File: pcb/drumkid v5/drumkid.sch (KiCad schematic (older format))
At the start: 51 parts, among them J5 Conn_01x05_Female, J6 Conn_01x04_Female, J7 Conn_01x06_Female, J8 Conn_01x05_Female, J9 AudioJack3_Ground_Switch, SW1 SW_SPDT, SW2 SW_Push, SW3 SW_Push, SW4 SW_Push, SW5 SW_Push, SW6 SW_Push, SW7 SW_Push, U2 ATmega328P-PU, U3 LM386, Y1 Crystal

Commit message: tidying up repo
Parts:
- C1, C2, C3, C7: renamed from C?; footprint (none) -> Capacitor_THT:C_Disc_D3.4mm_W2.1mm_P2.50mm
- J1: renamed from J?; footprint (none) -> Connector_PinHeader_2.54mm:PinHeader_1x02_P2.54mm_Vertical
- R1, R12, R13, R8: renamed from R?; footprint (none) -> Resistor_THT:R_Axial_DIN0207_L6.3mm_D2.5mm_P10.16mm_Horizontal
- RV1, RV2, RV3, RV4, RV5: footprint Potentiometer_THT:Potentiometer_Alps_RK09K_Single_Vertical -> drumkidcustom:Potentiometer_Alps_RK09K_Single_Vertical
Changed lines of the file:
@@
 F 0 "RV2" H 10230 3004 50  0000 R CNN
 F 1 "R_POT" H 10230 3095 50  0000 R CNN
-F 2 "Potentiometer_THT:Potentiometer_Alps_RK09K_Single_Vertical" H 10300 3050 50  0001 C CNN
+F 2 "drumkidcustom:Potentiometer_Alps_RK09K_Single_Vertical" H 10300 3050 50  0001 C CNN
 F 3 "~" H 10300 3050 50  0001 C CNN
 	1    10300 3050
@@
 F 0 "RV3" H 10230 3504 50  0000 R CNN
 F 1 "R_POT" H 10230 3595 50  0000 R CNN
-F 2 "Potentiometer_THT:Potentiometer_Alps_RK09K_Single_Vertical" H 10300 3550 50  0001 C CNN
+F 2 "drumkidcustom:Potentiometer_Alps_RK09K_Single_Vertical" H 10300 3550 50  0001 C CNN
 F 3 "~" H 10300 3550 50  0001 C CNN
 	1    10300 3550
@@
 F 0 "RV4" H 10230 4004 50  0000 R CNN
 F 1 "R_POT" H 10230 4095 50  0000 R CNN
-F 2 "Potentiometer_THT:Potentiometer_Alps_RK09K_Single_Vertical" H 10300 4050 50  0001 C CNN
+F 2 "drumkidcustom:Potentiometer_Alps_RK09K_Single_Vertical" H 10300 4050 50  0001 C CNN
 F 3 "~" H 10300 4050 50  0001 C CNN
 	1    10300 4050
@@
 F 0 "RV1" V 6243 850 50  0000 C CNN
 F 1 "10k" V 6334 850 50  0000 C CNN
-F 2 "Potentiometer_THT:Potentiometer_Alps_RK09K_Single_Vertical" H 6450 850 50  0001 C CNN
+F 2 "drumkidcustom:Potentiometer_Alps_RK09K_Single_Vertical" H 6450 850 50  0001 C CNN
 F 3 "~" H 6450 850 50  0001 C CNN
 	1    6450 850
@@
 F 0 "RV5" H 10230 4504 50  0000 R CNN
 F 1 "R_POT" H 10230 4595 50  0000 R CNN
-F 2 "Potentiometer_THT:Potentiometer_Alps_RK09K_Single_Vertical" H 10300 4550 50  0001 C CNN
+F 2 "drumkidcustom:Potentiometer_Alps_RK09K_Single_Vertical" H 10300 4550 50  0001 C CNN
 F 3 "~" H 10300 4550 50  0001 C CNN
 	1    10300 4550
@@
 	6950 1900 7150 1900
 $Comp
-L Connector:Conn_01x02_Female J?
+L Connector:Conn_01x02_Female J1
 U 1 1 5D8A22D2
 P 3500 5400
-F 0 "J?" H 3527 5376 50  0000 L CNN
+F 0 "J1" H 3527 5376 50  0000 L CNN
 F 1 "Conn_01x02_Female" H 3527 5285 50  0000 L CNN
-F 2 "" H 3500 5400 50  0001 C CNN
+F 2 "Connector_PinHeader_2.54mm:PinHeader_1x02_P2.54mm_Vertical" H 3500 5400 50  0001 C CNN
 F 3 "~" H 3500 5400 50  0001 C CNN
 	1    3500 5400
@@
 	3100 5500 3100 5700
 $Comp
-L Device:R R?
+L Device:R R1
 U 1 1 5D8A7D99
 P 4650 850
-F 0 "R?" V 4443 850 50  0000 C CNN
+F 0 "R1" V 4443 850 50  0000 C CNN
 F 1 "220" V 4534 850 50  0000 C CNN
-F 2 "" V 4580 850 50  0001 C CNN
+F 2 "Resistor_THT:R_Axial_DIN0207_L6.3mm_D2.5mm_P10.16mm_Horizontal" V 4580 850 50  0001 C CNN
 F 3 "~" H 4650 850 50  0001 C CNN
 	1    4650 850
@@
 $EndComp
 $Comp
-L Device:R R?
+L Device:R R8
 U 1 1 5D8A7E6C
 P 5450 850
-F 0 "R?" V 5243 850 50  0000 C CNN
+F 0 "R8" V 5243 850 50  0000 C CNN
 F 1 "680" V 5334 850 50  0000 C CNN
-F 2 "" V 5380 850 50  0001 C CNN
+F 2 "Resistor_THT:R_Axial_DIN0207_L6.3mm_D2.5mm_P10.16mm_Horizontal" V 5380 850 50  0001 C CNN
 F 3 "~" H 5450 850 50  0001 C CNN
 	1    5450 850
@@
 $EndComp
 $Comp
-L Device:R R?
+L Device:R R12
 U 1 1 5D8A7F2E
 P 5850 850
-F 0 "R?" V 5643 850 50  0000 C CNN
+F 0 "R12" V 5643 850 50  0000 C CNN
 F 1 "680" V 5734 850 50  0000 C CNN
-F 2 "" V 5780 850 50  0001 C CNN
+F 2 "Resistor_THT:R_Axial_DIN0207_L6.3mm_D2.5mm_P10.16mm_Horizontal" V 5780 850 50  0001 C CNN
 F 3 "~" H 5850 850 50  0001 C CNN
 	1    5850 850
@@
 $EndComp
 $Comp
-L Device:C C?
+L Device:C C1
 U 1 1 5D8A800B
 P 4850 1150
-F 0 "C?" H 4965 1196 50  0000 L CNN
+F 0 "C1" H 4965 1196 50  0000 L CNN
 F 1 "220nF" H 4965 1105 50  0000 L CNN
-F 2 "" H 4888 1000 50  0001 C CNN
+F 2 "Capacitor_THT:C_Disc_D3.4mm_W2.1mm_P2.50mm" H 4888 1000 50  0001 C CNN
 F 3 "~" H 4850 1150 50  0001 C CNN
 	1    4850 1150
@@
 $EndComp
 $Comp
-L Device:C C?
+L Device:C C3
 U 1 1 5D8BB366
 P 5650 1150
-F 0 "C?" H 5765 1196 50  0000 L CNN
+F 0 "C3" H 5765 1196 50  0000 L CNN
 F 1 "1nF" H 5765 1105 50  0000 L CNN
-F 2 "" H 5688 1000 50  0001 C CNN
+F 2 "Capacitor_THT:C_Disc_D3.4mm_W2.1mm_P2.50mm" H 5688 1000 50  0001 C CNN
 F 3 "~" H 5650 1150 50  0001 C CNN
 	1    5650 1150
@@
 	6000 850  6050 850
 $Comp
-L Device:C C?
+L Device:C C7
 U 1 1 5D8C53A5
 P 6050 1150
-F 0 "C?" H 6165 1196 50  0000 L CNN
+F 0 "C7" H 6165 1196 50  0000 L CNN
 F 1 "220nF" H 6165 1105 50  0000 L CNN
-F 2 "" H 6088 1000 50  0001 C CNN
+F 2 "Capacitor_THT:C_Disc_D3.4mm_W2.1mm_P2.50mm" H 6088 1000 50  0001 C CNN
 F 3 "~" H 6050 1150 50  0001 C CNN
 	1    6050 1150
@@
 $EndComp
 $Comp
-L Device:C C?
+L Device:C C2
 U 1 1 5D8C5552
 P 5250 1150
-F 0 "C?" H 5365 1196 50  0000 L CNN
+F 0 "C2" H 5365 1196 50  0000 L CNN
 F 1 "220nF" H 5365 1105 50  0000 L CNN
-F 2 "" H 5288 1000 50  0001 C CNN
+F 2 "Capacitor_THT:C_Disc_D3.4mm_W2.1mm_P2.50mm" H 5288 1000 50  0001 C CNN
 F 3 "~" H 5250 1150 50  0001 C CNN
 	1    5250 1150
@@
 	6050 1450 6050 1300
 $Comp
-L Device:R R?
+L Device:R R13
 U 1 1 5D8CABE9
 P 6050 1650
-F 0 "R?" H 6120 1696 50  0000 L CNN
+F 0 "R13" H 6120 1696 50  0000 L CNN
 F 1 "330" H 6120 1605 50  0000 L CNN
-F 2 "" V 5980 1650 50  0001 C CNN
+F 2 "Resistor_THT:R_Axial_DIN0207_L6.3mm_D2.5mm_P10.16mm_Horizontal" V 5980 1650 50  0001 C CNN
 F 3 "~" H 6050 1650 50  0001 C CNN
 	1    6050 1650
@@
 	4850 1300 4850 1900
 Wire Wire Line
-	4850 1900 5650 1900
+	4850 1900 5300 1900
 Connection ~ 4850 1900
 Wire Wire Line
@@
 Wire Wire Line
 	6050 850  6300 850
+$Comp
+L power:PWR_FLAG #FLG0101
+U 1 1 5D8894D3
+P 5300 1900
+F 0 "#FLG0101" H 5300 1975 50  0001 C CNN
+F 1 "PWR_FLAG" H 5300 2074 50  0000 C CNN
+F 2 "" H 5300 1900 50  0001 C CNN
+F 3 "~" H 5300 1900 50  0001 C CNN
+	1    5300 1900
+	1    0    0    -1
+$EndComp
+Connection ~ 5300 1900
+Wire Wire Line
+	5300 1900 5650 1900
 $EndSCHEMATC

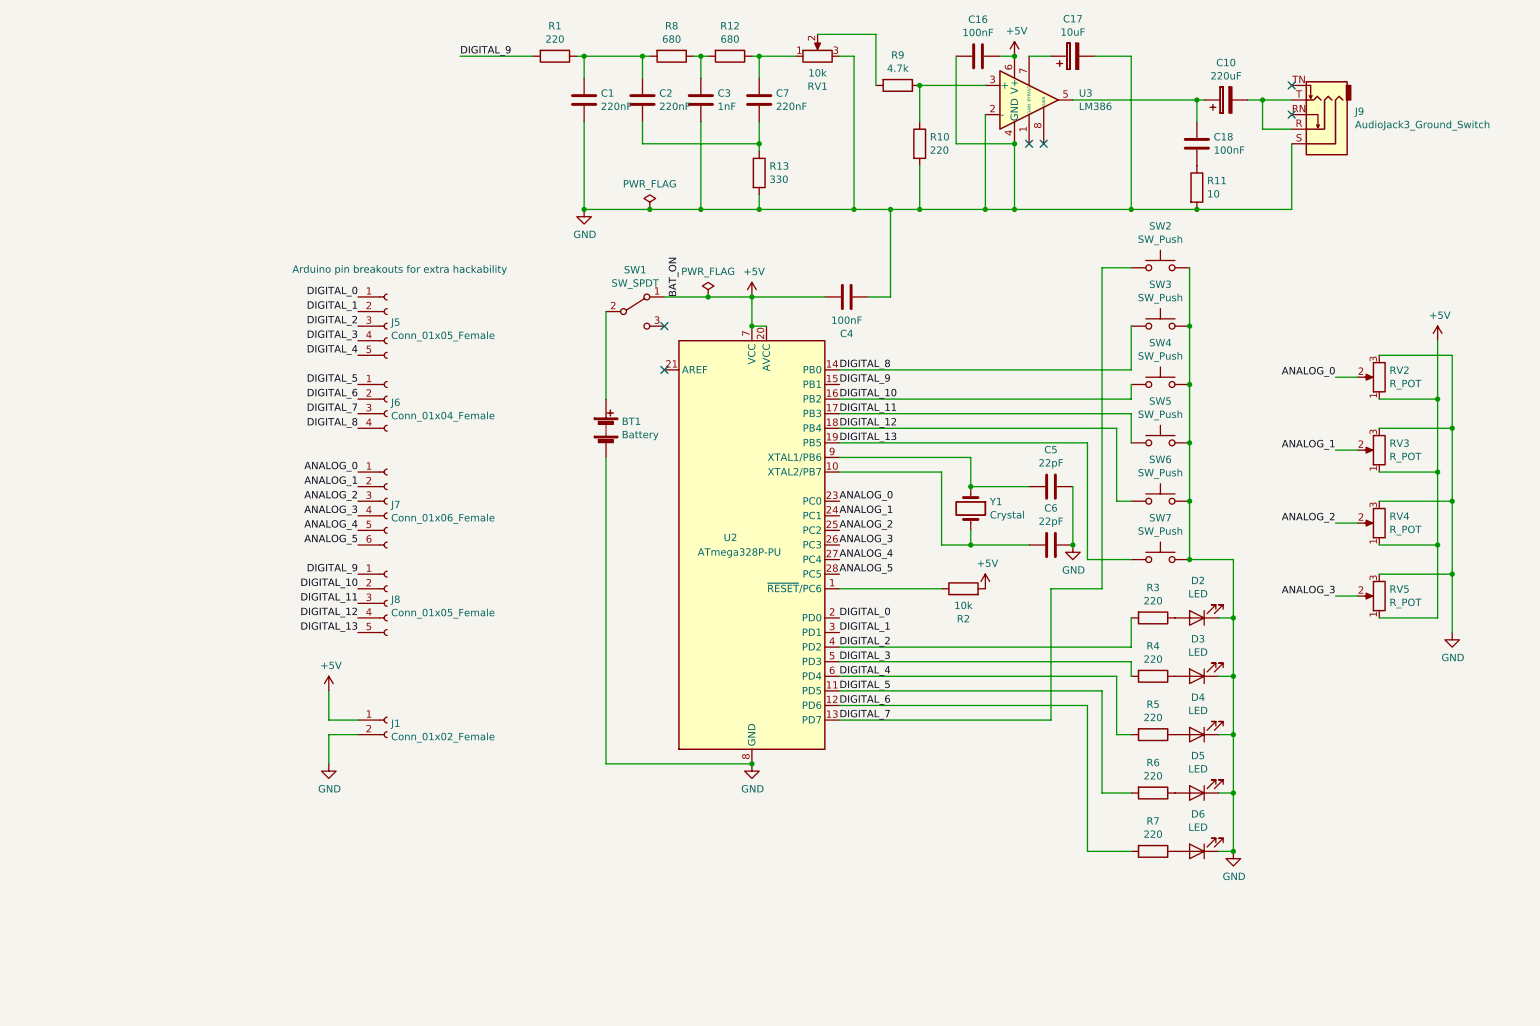
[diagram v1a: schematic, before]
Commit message: lots of new stuff - pcb v5 progress, midi code progress, but lots to be done
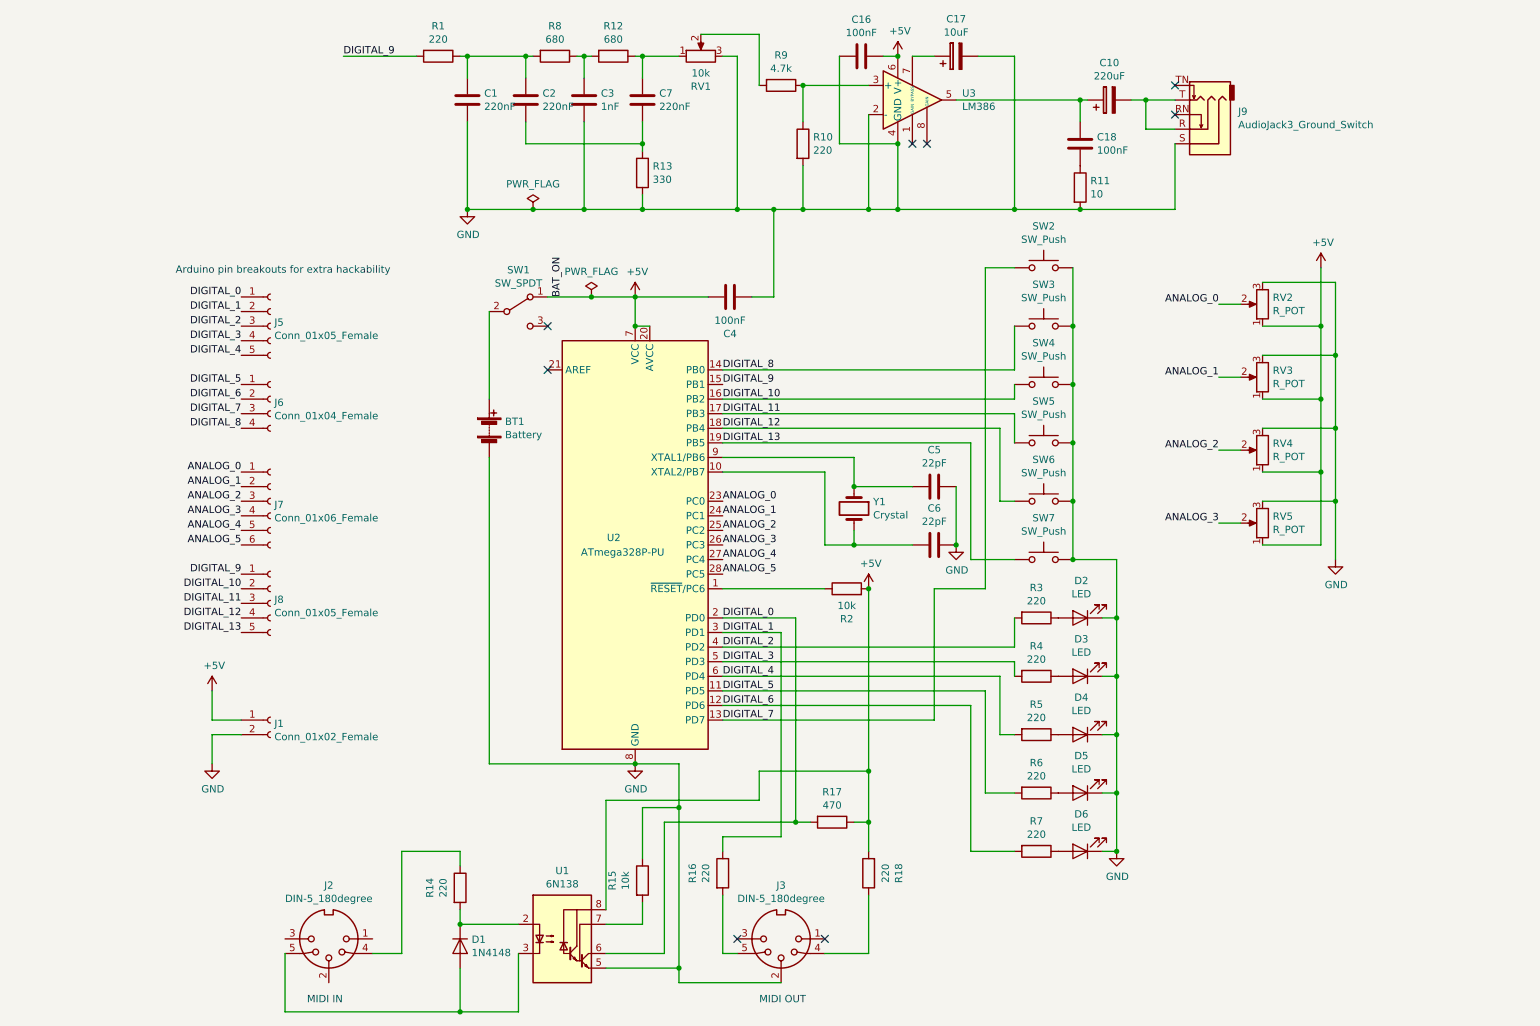
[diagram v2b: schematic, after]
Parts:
- added D1: 1N4148, Diode_THT:D_DO-35_SOD27_P7.62mm_Horizontal, symbol Diode:1N4148
- added J2, J3: DIN-5_180degree, Eurocad:MIDI_DIN5, symbol Connector:DIN-5_180degree
- added R14, R16, R18: 220, Resistor_THT:R_Axial_DIN0207_L6.3mm_D2.5mm_P10.16mm_Horizontal, symbol Device:R
- added R15: 10k, Resistor_THT:R_Axial_DIN0207_L6.3mm_D2.5mm_P10.16mm_Horizontal, symbol Device:R
- added R17: 470, Resistor_THT:R_Axial_DIN0207_L6.3mm_D2.5mm_P10.16mm_Horizontal, symbol Device:R
- added U1: 6N138, Package_DIP:DIP-8_W7.62mm_Socket, symbol Isolator:6N138
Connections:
- net +5V: now also R17.1, R18.2, U1.8 (VCC)
- net DIGITAL_0: now also R17.2, U1.6 (VO2)
- net DIGITAL_1: now also R16.1
- net GND: now also J3.2, R15.1, U1.5 (GND)
- new net: J3.4, R18.1
- new net: J3.5, R16.2
- new net: J2.4, R14.1
- new net: D1.2 (A), J2.5, U1.3 (C2)
- new net: D1.1 (K), R14.2, U1.2 (C1)
- new net: R15.2, U1.7 (VO1)
- no-connect marks 6 -> 8
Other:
- note added: "MIDI IN"
- note added: "MIDI OUT"
- moved on the sheet: BT1, C1, C10, C16, C17, C18, C2, C3, C4, C5, C6, C7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

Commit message: more pcb progress
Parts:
- added D?: LED, LED_THT:LED_D5.0mm, symbol Device:LED
- added R?: 220, Resistor_THT:R_Axial_DIN0207_L6.3mm_D2.5mm_P10.16mm_Horizontal, symbol Device:R
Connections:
- net GND: now also D?.1 (K), R?.2
- new net: D?.2 (A), R?.1
- no-connect marks 8 -> 11
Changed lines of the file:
@@
 Connection ~ 7000 1900
 Wire Wire Line
-	7000 1900 7800 1900
+	7000 1900 7150 1900
 Connection ~ 10000 3900
 Wire Wire Line
@@
 Wire Wire Line
 	6800 5750 6800 4500
+$Comp
+L Device:LED D?
+U 1 1 5DBB8A3C
+P 6850 2500
+F 0 "D?" H 6842 2245 50  0000 C CNN
+F 1 "LED" H 6842 2336 50  0000 C CNN
+F 2 "LED_THT:LED_D5.0mm" H 6850 2500 50  0001 C CNN
+F 3 "~" H 6850 2500 50  0001 C CNN
+	1    6850 2500
+	-1   0    0    1
+$EndComp
+$Comp
+L Device:R R?
+U 1 1 5DBB8B2A
+P 6450 2500
+F 0 "R?" V 6243 2500 50  0000 C CNN
+F 1 "220" V 6334 2500 50  0000 C CNN
+F 2 "Resistor_THT:R_Axial_DIN0207_L6.3mm_D2.5mm_P10.16mm_Horizontal" V 6380 2500 50  0001 C CNN
+F 3 "~" H 6450 2500 50  0001 C CNN
+	1    6450 2500
+	0    1    1    0
+$EndComp
+Wire Wire Line
+	7000 2500 7150 2500
+Wire Wire Line
+	7150 2500 7150 1900
+Connection ~ 7150 1900
+Wire Wire Line
+	7150 1900 7800 1900
+Wire Wire Line
+	6150 2500 6300 2500
+Connection ~ 6150 2500
+Wire Wire Line
+	6600 2500 6700 2500
+NoConn ~ 3100 7200
+NoConn ~ 3400 6900
+NoConn ~ 2800 6900
 $EndSCHEMATC

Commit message: more pcb stuff
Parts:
- added H1, H2, H3, H4, H5, H6: MountingHole, MountingHole:MountingHole_3.2mm_M3, symbol Mechanical:MountingHole
- BT1: footprint Connector_PinHeader_2.54mm:PinHeader_1x02_P2.54mm_Vertical -> Connector_Wire:SolderWirePad_1x02_P5.08mm_Drill1.5mm
- gave numbers to parts that had none: 2
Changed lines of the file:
@@
 F 0 "BT1" H 4308 3446 50  0000 L CNN
 F 1 "Battery" H 4308 3355 50  0000 L CNN
-F 2 "Connector_PinHeader_2.54mm:PinHeader_1x02_P2.54mm_Vertical" V 4200 3460 50  0001 C CNN
+F 2 "Connector_Wire:SolderWirePad_1x02_P5.08mm_Drill1.5mm" V 4200 3460 50  0001 C CNN
 F 3 "~" V 4200 3460 50  0001 C CNN
 	1    4200 3400
@@
 	6800 5750 6800 4500
 $Comp
-L Device:LED D?
+L Device:LED D7
 U 1 1 5DBB8A3C
 P 6850 2500
-F 0 "D?" H 6842 2245 50  0000 C CNN
+F 0 "D7" H 6842 2245 50  0000 C CNN
 F 1 "LED" H 6842 2336 50  0000 C CNN
 F 2 "LED_THT:LED_D5.0mm" H 6850 2500 50  0001 C CNN
@@
 $EndComp
 $Comp
-L Device:R R?
+L Device:R R19
 U 1 1 5DBB8B2A
 P 6450 2500
-F 0 "R?" V 6243 2500 50  0000 C CNN
+F 0 "R19" V 6243 2500 50  0000 C CNN
 F 1 "220" V 6334 2500 50  0000 C CNN
 F 2 "Resistor_THT:R_Axial_DIN0207_L6.3mm_D2.5mm_P10.16mm_Horizontal" V 6380 2500 50  0001 C CNN
@@
 NoConn ~ 3400 6900
 NoConn ~ 2800 6900
+$Comp
+L Mechanical:MountingHole H1
+U 1 1 5DB7E4A0
+P 1000 800
+F 0 "H1" H 1100 846 50  0000 L CNN
+F 1 "MountingHole" H 1100 755 50  0000 L CNN
+F 2 "MountingHole:MountingHole_3.2mm_M3" H 1000 800 50  0001 C CNN
+F 3 "~" H 1000 800 50  0001 C CNN
+	1    1000 800
+	1    0    0    -1
+$EndComp
+$Comp
+L Mechanical:MountingHole H2
+U 1 1 5DB7E63A
+P 1000 1000
+F 0 "H2" H 1100 1046 50  0000 L CNN
+F 1 "MountingHole" H 1100 955 50  0000 L CNN
+F 2 "MountingHole:MountingHole_3.2mm_M3" H 1000 1000 50  0001 C CNN
+F 3 "~" H 1000 1000 50  0001 C CNN
+	1    1000 1000
+	1    0    0    -1
+$EndComp
+$Comp
+L Mechanical:MountingHole H3
+U 1 1 5DB7E762
+P 1000 1200
+F 0 "H3" H 1100 1246 50  0000 L CNN
+F 1 "MountingHole" H 1100 1155 50  0000 L CNN
+F 2 "MountingHole:MountingHole_3.2mm_M3" H 1000 1200 50  0001 C CNN
+F 3 "~" H 1000 1200 50  0001 C CNN
+	1    1000 1200
+	1    0    0    -1
+$EndComp
+$Comp
+L Mechanical:MountingHole H4
+U 1 1 5DB7E7F8
+P 1000 1400
+F 0 "H4" H 1100 1446 50  0000 L CNN
+F 1 "MountingHole" H 1100 1355 50  0000 L CNN
+F 2 "MountingHole:MountingHole_3.2mm_M3" H 1000 1400 50  0001 C CNN
+F 3 "~" H 1000 1400 50  0001 C CNN
+	1    1000 1400
+	1    0    0    -1
+$EndComp
+$Comp
+L Mechanical:MountingHole H5
+U 1 1 5DB7E890
+P 1000 1600
+F 0 "H5" H 1100 1646 50  0000 L CNN
+F 1 "MountingHole" H 1100 1555 50  0000 L CNN
+F 2 "MountingHole:MountingHole_3.2mm_M3" H 1000 1600 50  0001 C CNN
+F 3 "~" H 1000 1600 50  0001 C CNN
+	1    1000 1600
+	1    0    0    -1
+$EndComp
+$Comp
+L Mechanical:MountingHole H6
+U 1 1 5DB7E92E
+P 1000 1800
+F 0 "H6" H 1100 1846 50  0000 L CNN
+F 1 "MountingHole" H 1100 1755 50  0000 L CNN
+F 2 "MountingHole:MountingHole_3.2mm_M3" H 1000 1800 50  0001 C CNN
+F 3 "~" H 1000 1800 50  0001 C CNN
+	1    1000 1800
+	1    0    0    -1
+$EndComp
 $EndSCHEMATC

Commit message: and more pcb stuff
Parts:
- added H7, H8: MountingHole, MountingHole:MountingHole_3.2mm_M3, symbol Mechanical:MountingHole
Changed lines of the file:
@@
 Wire Wire Line
 	9200 3550 9350 3550
-NoConn ~ 4600 2700
 $Comp
 L Connector:AudioJack3_Ground_Switch J9
@@
 	0    -1   -1   0
 $EndComp
-Wire Wire Line
-	4600 2500 4900 2500
 Connection ~ 5200 2500
-Connection ~ 4900 2500
 Wire Wire Line
 	4900 2500 5200 2500
-Wire Wire Line
-	4200 2600 4200 3200
 Wire Wire Line
 	4200 3600 4200 5700
@@
 	1    0    0    -1
 $EndComp
+$Comp
+L Mechanical:MountingHole H7
+U 1 1 5DB7F9BD
+P 1000 2200
+F 0 "H7" H 1100 2246 50  0000 L CNN
+F 1 "MountingHole" H 1100 2155 50  0000 L CNN
+F 2 "MountingHole:MountingHole_3.2mm_M3" H 1000 2200 50  0001 C CNN
+F 3 "~" H 1000 2200 50  0001 C CNN
+	1    1000 2200
+	1    0    0    -1
+$EndComp
+$Comp
+L Mechanical:MountingHole H8
+U 1 1 5DB7FA6B
+P 1000 2400
+F 0 "H8" H 1100 2446 50  0000 L CNN
+F 1 "MountingHole" H 1100 2355 50  0000 L CNN
+F 2 "MountingHole:MountingHole_3.2mm_M3" H 1000 2400 50  0001 C CNN
+F 3 "~" H 1000 2400 50  0001 C CNN
+	1    1000 2400
+	1    0    0    -1
+$EndComp
+Wire Wire Line
+	4200 2600 4200 3200
+Connection ~ 4900 2500
+Wire Wire Line
+	4600 2500 4900 2500
+NoConn ~ 4600 2700
 $EndSCHEMATC

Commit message: finished messing about with pcb layout, next comes routing...
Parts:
- C1, C16, C18, C2, C3, C4, C5, C6, C7: footprint Capacitor_THT:C_Disc_D3.4mm_W2.1mm_P2.50mm -> drumkidcustom:C_Disc_D3.4mm_W2.1mm_P2.50mm
- C10, C17: footprint Capacitor_THT:CP_Radial_D6.3mm_P2.50mm -> drumkidcustom:CP_Radial_D6.3mm_P2.50mm
- D2, D3, D4, D5, D6, D7: footprint LED_THT:LED_D5.0mm -> drumkidcustom:LED_D5.0mm
- H1, H2, H3, H4, H5, H6, H7, H8: footprint MountingHole:MountingHole_3.2mm_M3 -> drumkidcustom:MountingHole_3.2mm_M3
- J2, J3: footprint Eurocad:MIDI_DIN5 -> drumkidcustom:MIDI_DIN5
- J9: footprint headphone:Tayda_3.5mm_stereo_TRS_jack_A-853 -> drumkidcustom:Tayda_3.5mm_stereo_TRS_jack_A-853
- R1, R10, R11, R12, R13, R14, R15, R16, R17, R18, R19, R2, R3, R4, R5, R6, R7, R8, R9: footprint Resistor_THT:R_Axial_DIN0207_L6.3mm_D2.5mm_P10.16mm_Horizontal -> drumkidcustom:R_Axial_DIN0207_L6.3mm_D2.5mm_P10.16mm_Horizontal
- SW1: footprint SamacSys_Parts:EG1206 -> drumkidcustom:EG1206
- SW2, SW3, SW4, SW5, SW6, SW7: footprint Button_Switch_THT:SW_PUSH-12mm_Wuerth-430476085716 -> drumkidcustom:SW_PUSH-12mm_Wuerth-430476085716
